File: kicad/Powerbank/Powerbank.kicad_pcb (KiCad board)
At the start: 4 copper layers, 90 x 60 mm, 166 parts, among them IC1 BQ4050RSMR, IC2 SN74LVC1G14DSFR, IC3 SN74LVC1G08DSFR, IC4 BQ25703ARSNT, IC5 TPD6S300ARUKR, IC6 W25Q80DVSNIG, J1 USB_C_Receptacle, J2 USB_A, J3 Conn_01x02_Male, J4 Conn_01x05_Male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

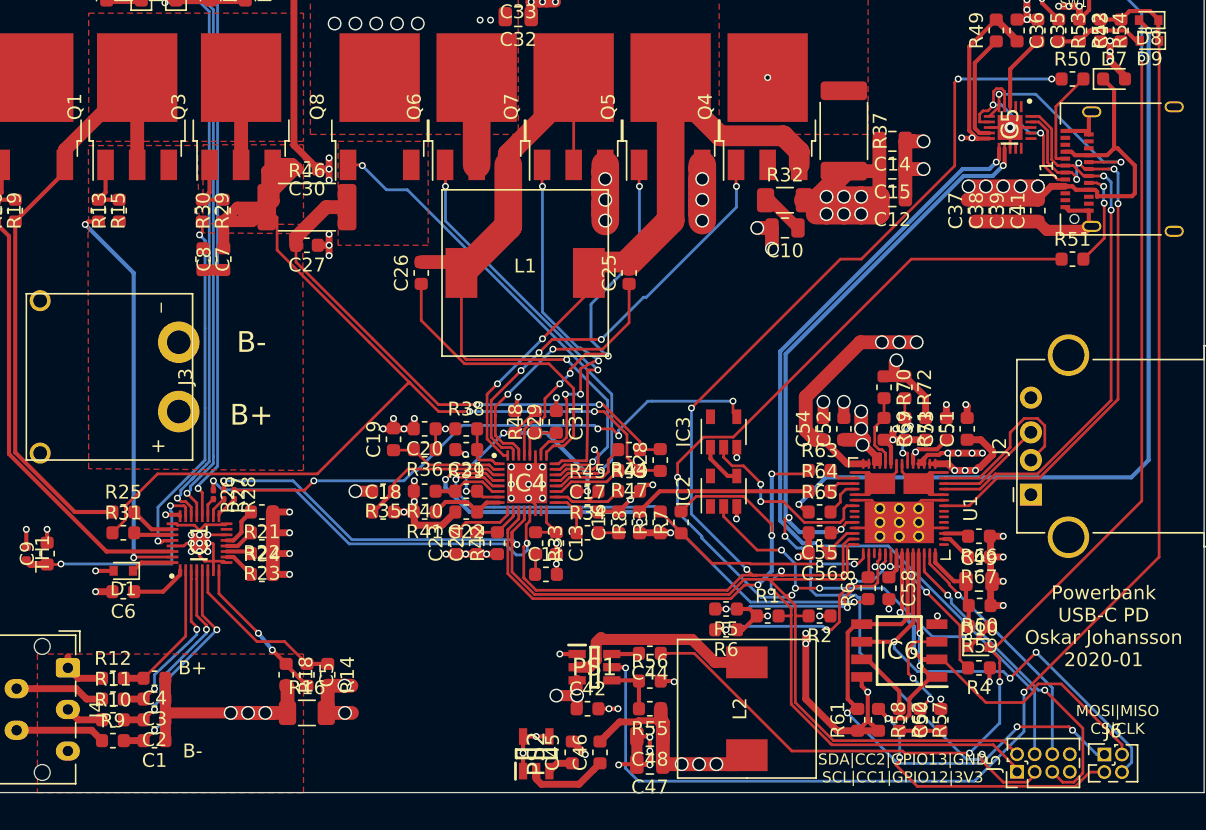
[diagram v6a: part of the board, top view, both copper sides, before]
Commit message: DRC almost finished and added cap for USB-A
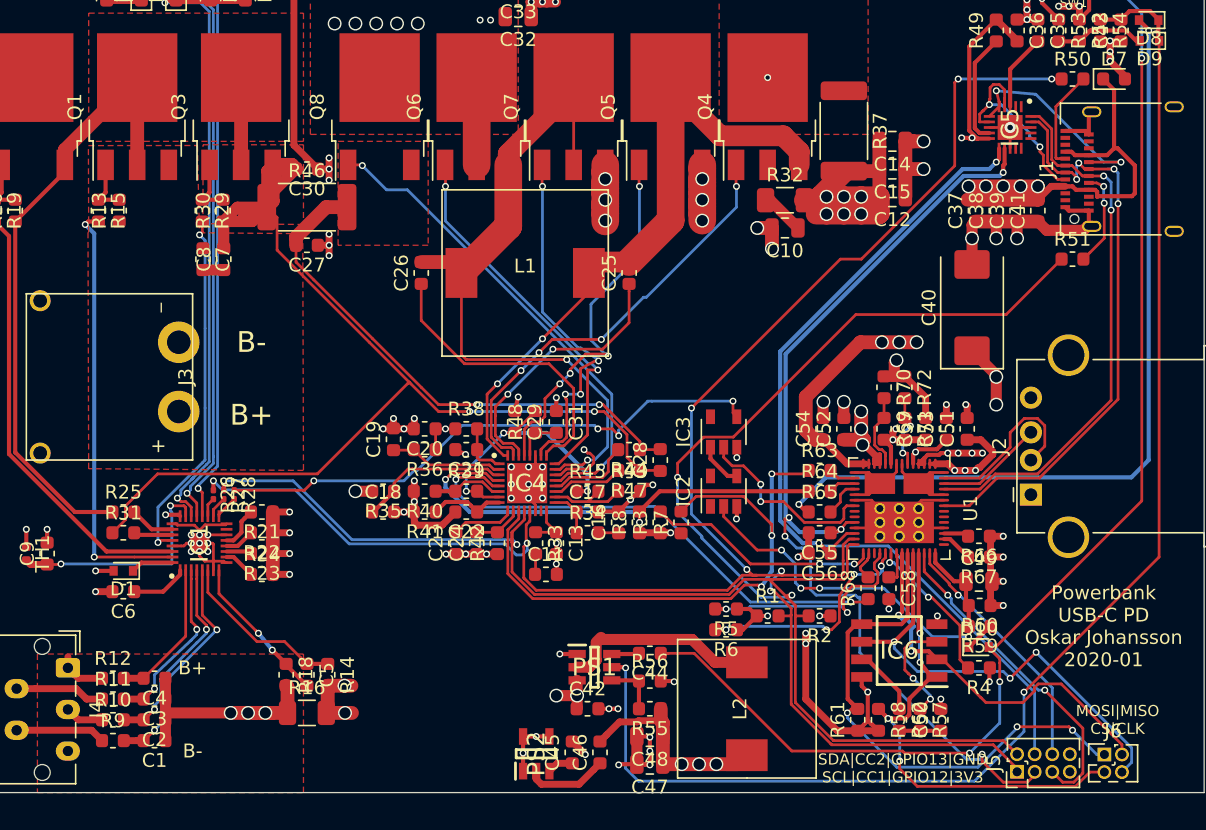
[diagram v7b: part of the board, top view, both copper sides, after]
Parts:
- added C40: 100µF, Capacitor_Tantalum_SMD:CP_EIA-7343-15_Kemet-W, F.Cu at (173.2, 95.0)
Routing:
- net VBUS_A: track 13.0 -> 23.1 mm, vias 4 -> 6
- net GND: track 150.9 -> 156.5 mm, vias 79 -> 82
- net Net-(IC1-Pad31): track 29.4 -> 31.0 mm
- net TP6: track 29.2 -> 28.2 mm
- net Net-(IC1-Pad28): track 26.6 -> 25.8 mm
- net SYS: track 152.3 -> 151.5 mm
- net CC1_CONN: track 14.3 -> 15.1 mm
- net SCL_2: track 15.7 -> 16.5 mm, vias 3 -> 2
- net Net-(R68-Pad2): track 1.76 -> 2.30 mm
- net SPI_MISO: track 27.8 -> 28.3 mm

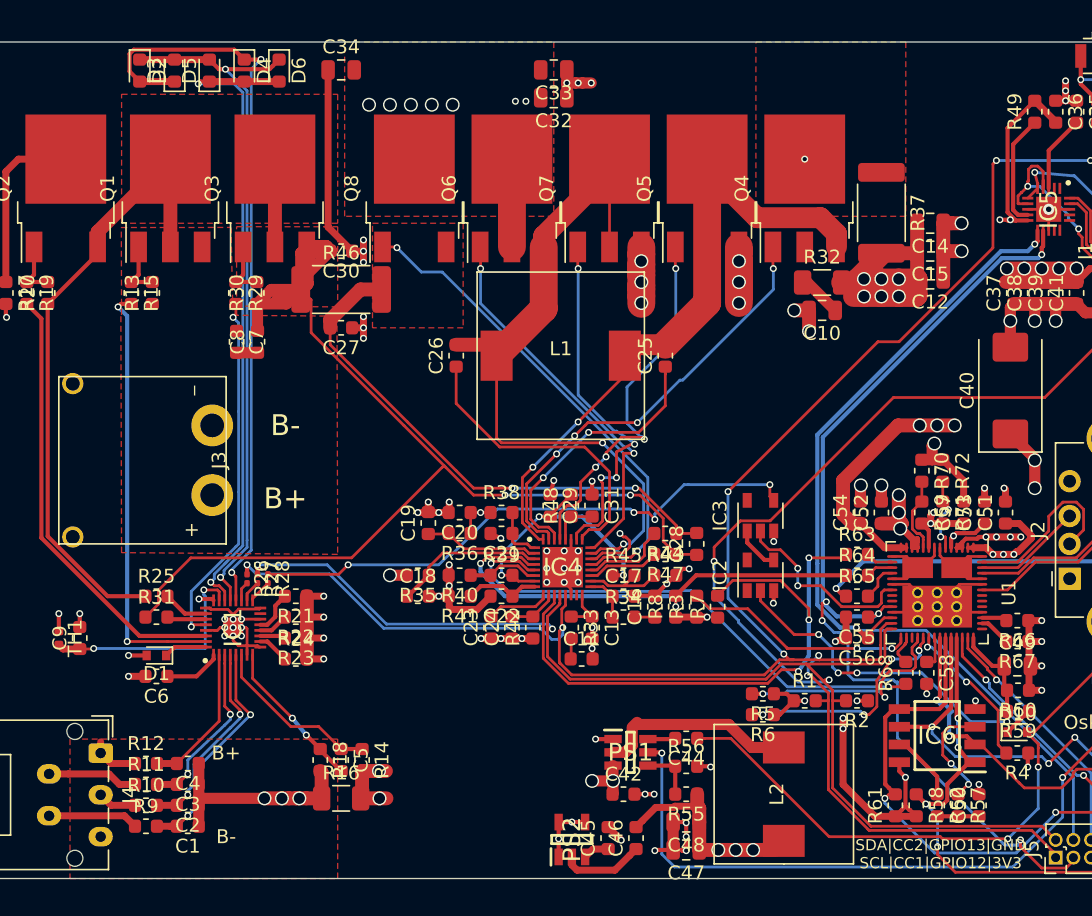
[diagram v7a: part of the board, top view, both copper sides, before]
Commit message: Double checked footprint for IC and Mosfets
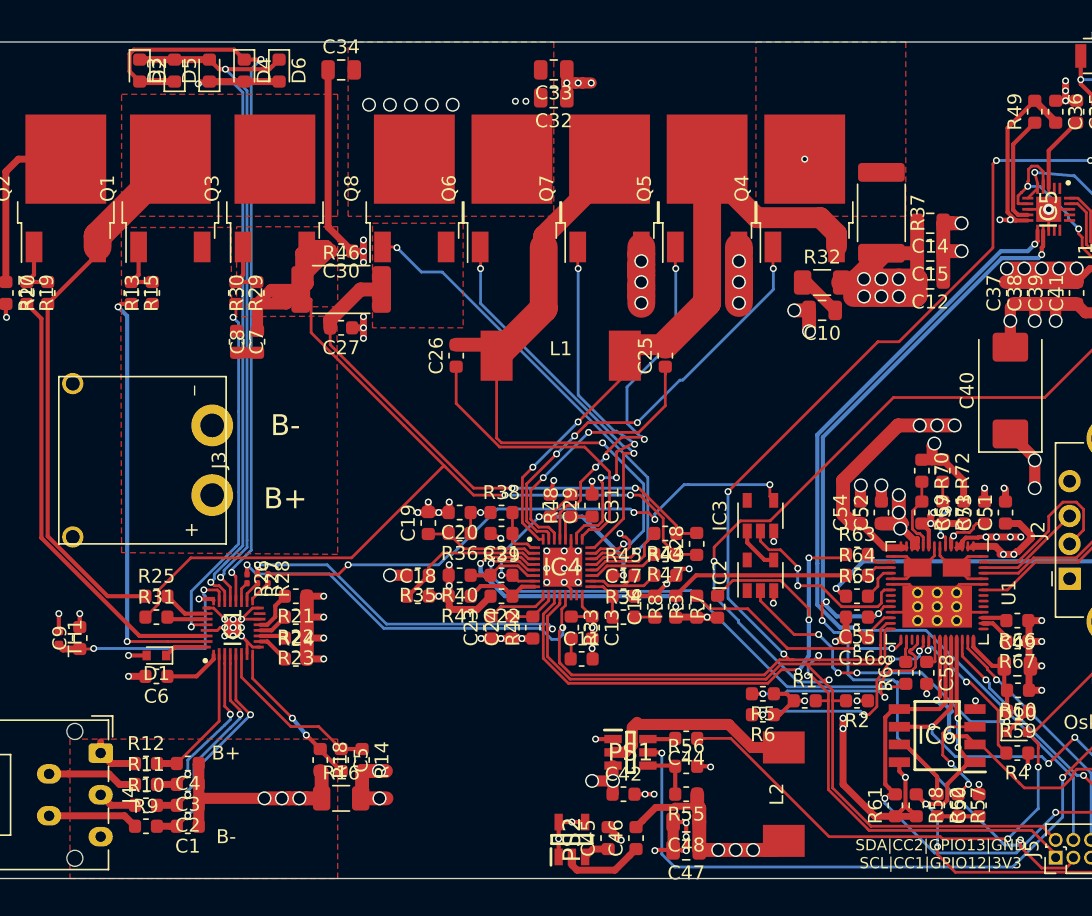
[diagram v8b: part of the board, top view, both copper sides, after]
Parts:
- Q1, Q3, Q4, Q5, Q6, Q7: footprint Package_TO_SOT_SMD:TO-252-3_TabPin2 -> Package_TO_SOT_SMD:TO-252-2
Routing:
- net /Cell Balancer BQ4050/Source: track 52.1 -> 39.5 mm
- net TP2: track 52.6 -> 46.3 mm
- net SYS: track 151.5 -> 145.2 mm
- net -BATT: track 41.7 -> 39.9 mm
- net VBUS_C: track 71.3 -> 72.8 mm
- net PD_LDO_3V3: track 116.2 -> 117.0 mm
- net Net-(R67-Pad2): track 2.28 -> 2.81 mm
- net +5V: track 54.4 -> 54.7 mm, vias 6 -> 5
